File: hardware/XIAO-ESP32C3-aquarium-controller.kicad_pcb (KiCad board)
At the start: 2 copper layers, 70 x 100 mm, 43 parts, among them J1 Conn_01x02, J2 Conn_01x07, J3 Conn_01x06, J4 Conn_01x03, J5 Conn_01x03, K1 SANYOU_SRD_Form_C, K2 SANYOU_SRD_Form_C, K3 SANYOU_SRD_Form_C, Q1 AO3400A, Q2 AO3400A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

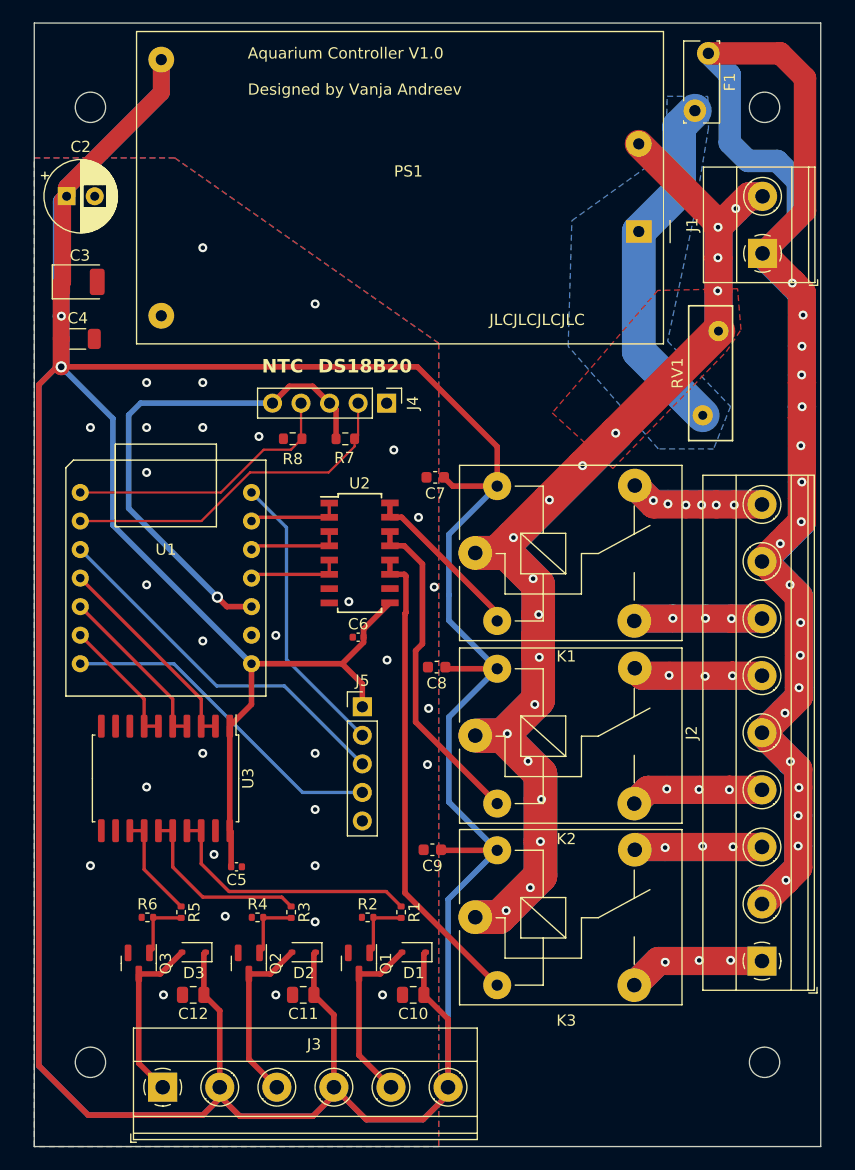
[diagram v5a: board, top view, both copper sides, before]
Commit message: changes in pcb size and holes for case fitting
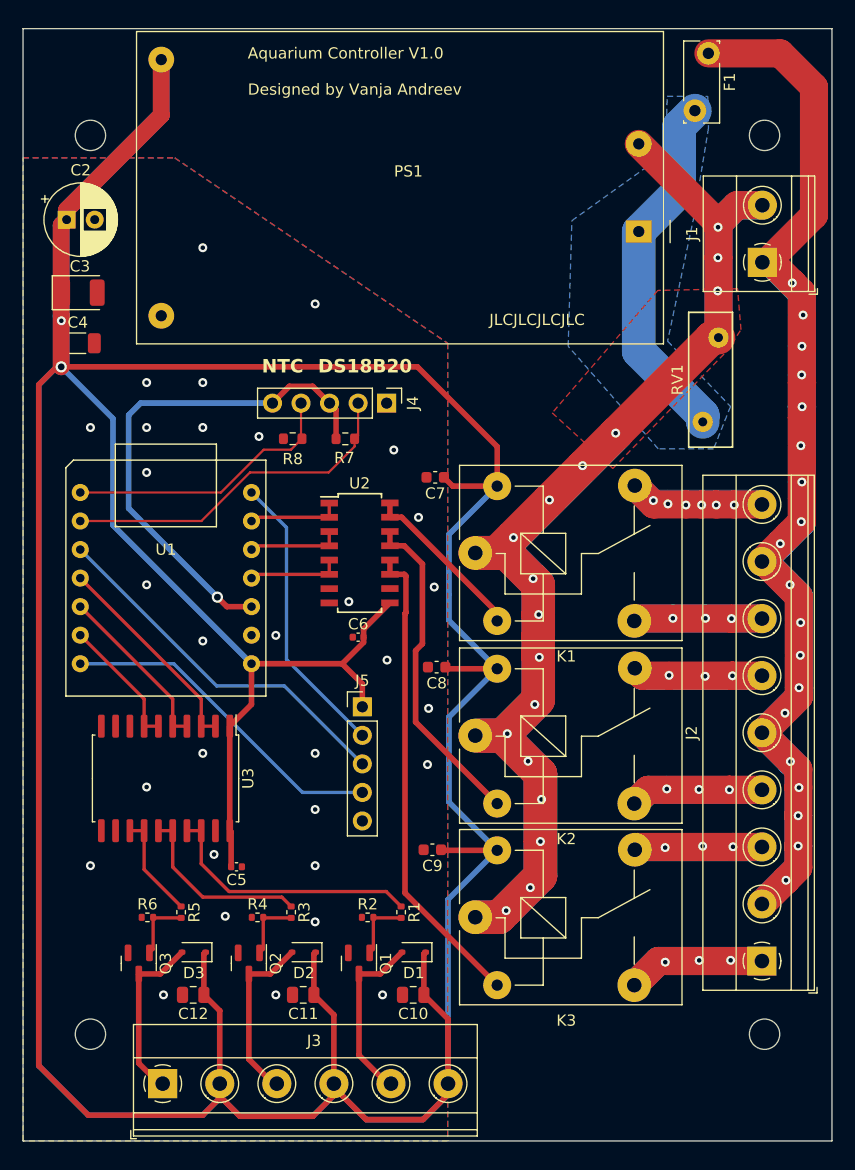
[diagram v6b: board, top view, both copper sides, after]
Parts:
- moved H1 2.50 mm to (36.6, 37.0)
- moved H2 2.50 mm to (96.6, 37.0)
- moved H3 2.50 mm to (36.6, 117.0)
- moved H4 2.50 mm to (96.6, 117.0)
- moved C2 2.08 mm to (34.5, 44.5)
- moved C3 0.96 mm to (35.7, 51.0)
- moved J1 0.79 mm to (96.4, 48.3)
- moved RV1 0.58 mm to (92.5, 55.0)
- moved C4 0.38 mm to (35.5, 55.5)
- moved J3 0.32 mm to (43.0, 121.4)
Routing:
- net AL/L: track 181.1 -> 157.1 mm
- net Net-(PS1-AC/L): track 31.5 -> 32.1 mm
- net AL/N: track 175.4 -> 175.0 mm, vias 18 -> 17
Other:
- board size 70 x 100 mm -> 72 x 99 mm

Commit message: changes in AC tracks
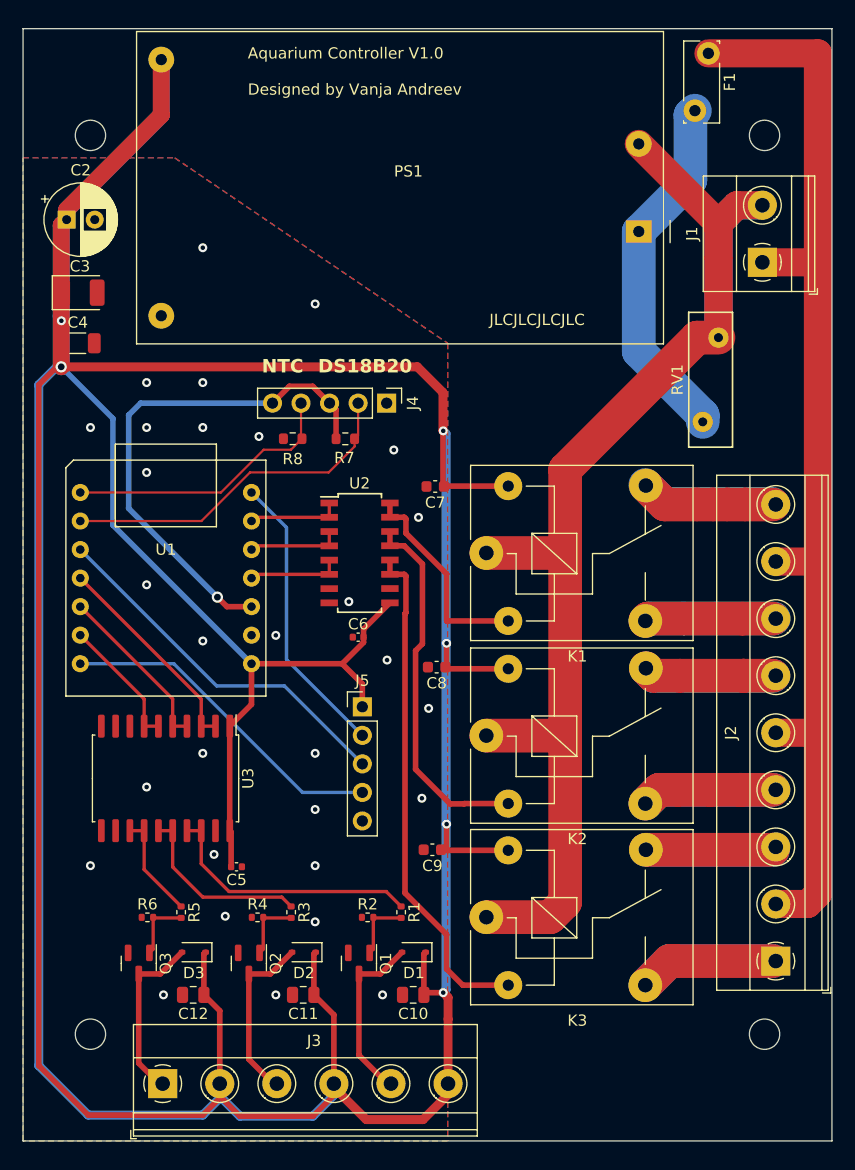
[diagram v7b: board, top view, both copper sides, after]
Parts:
- moved J2 1.23 mm to (97.6, 110.5)
- moved K1 0.98 mm to (71.8, 74.2)
- moved K2 0.98 mm to (71.8, 90.4)
- moved K3 0.98 mm to (71.8, 106.6)
- moved C7 0.81 mm to (67.3, 68.2)
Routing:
- net AL/N: track 175.0 -> 117.0 mm, vias 17 -> 0
- net AL/L: track 157.1 -> 101.5 mm, vias 19 -> 0
- net +5V: track 513.0 -> 507.4 mm, vias 2 -> 6
- net /rel1: track 15.1 -> 19.5 mm
- net /rel2: track 29.4 -> 32.9 mm
- net /rel3: track 42.6 -> 45.4 mm
- net /Relay3/NO: track 22.6 -> 23.3 mm, vias 3 -> 0
- net /Relay2/NO: vias 3 -> 0
- net /Relay2/NC: vias 3 -> 0
- net /Relay1/NC: vias 3 -> 0
- net GND: vias 31 -> 30
- net /Relay3/NC: vias 3 -> 0
- net /Relay1/NO: vias 6 -> 0
- removed copper zone on F.Cu, net AL/N
- removed copper zone on B.Cu, net Net-(PS1-AC/L)

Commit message: changes in tracks, spacing....
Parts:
- moved J2 0.40 mm to (97.2, 110.5)
- moved K1 0.15 mm to (71.7, 74.2)
- moved K2 0.15 mm to (71.7, 90.4)
- moved K3 0.15 mm to (71.7, 106.6)
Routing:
- net /Relay3/NO: track 23.3 -> 11.3 mm
- net /Relay2/NC: track 23.5 -> 11.7 mm
- net /Relay3/NC: track 24.1 -> 12.3 mm
- net /Relay2/NO: track 23.1 -> 11.4 mm
- net /Relay1/NC: track 22.8 -> 11.2 mm
- net /Relay1/NO: track 23.2 -> 11.8 mm
- net AL/L: track 101.5 -> 96.9 mm
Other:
- outline, holes or cut-outs redrawn
